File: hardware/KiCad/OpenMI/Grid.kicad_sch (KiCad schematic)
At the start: 21 parts, among them U2 MCP6002-SN

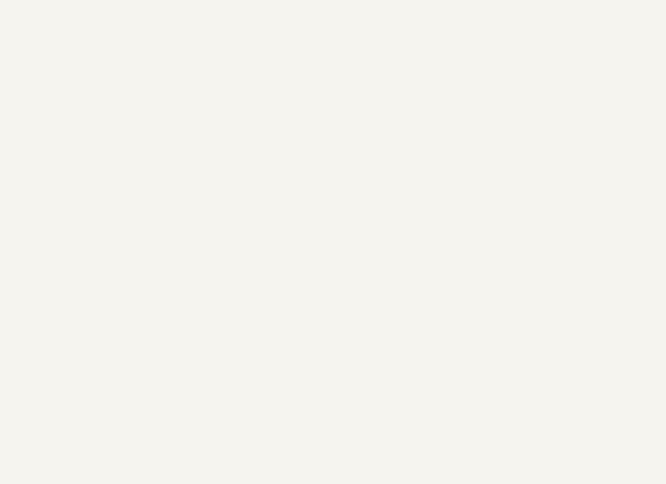
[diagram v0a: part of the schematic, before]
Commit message: feat: Adds surge and burst protection
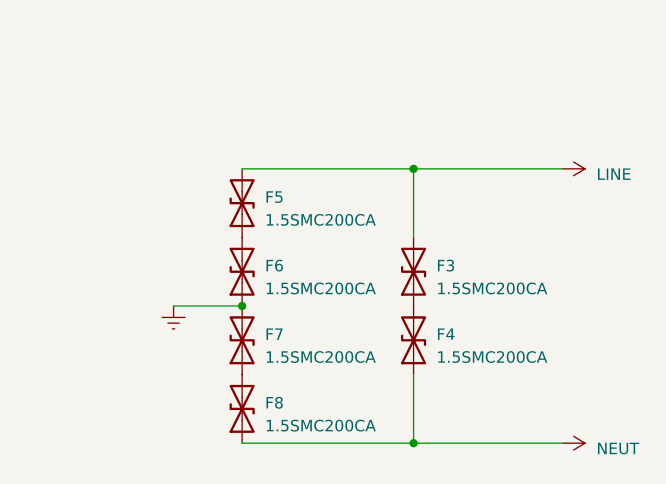
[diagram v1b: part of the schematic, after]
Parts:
- added F3, F4, F5, F6, F7, F8: 1.5SMC200CA, Diode_SMD:D_SMC, symbol _Diode_TVS:1.5SMC200CA
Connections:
- net LINE: now also F3.2 (A2), F5.2 (A2)
- net NEUT: now also F4.1 (A1), F8.1 (A1)
- new net: F7.1 (A1), F8.2 (A2)
- new net: F5.1 (A1), F6.2 (A2)
- new net: F3.1 (A1), F4.2 (A2)
- new net Earth: F6.1 (A1), F7.2 (A2)

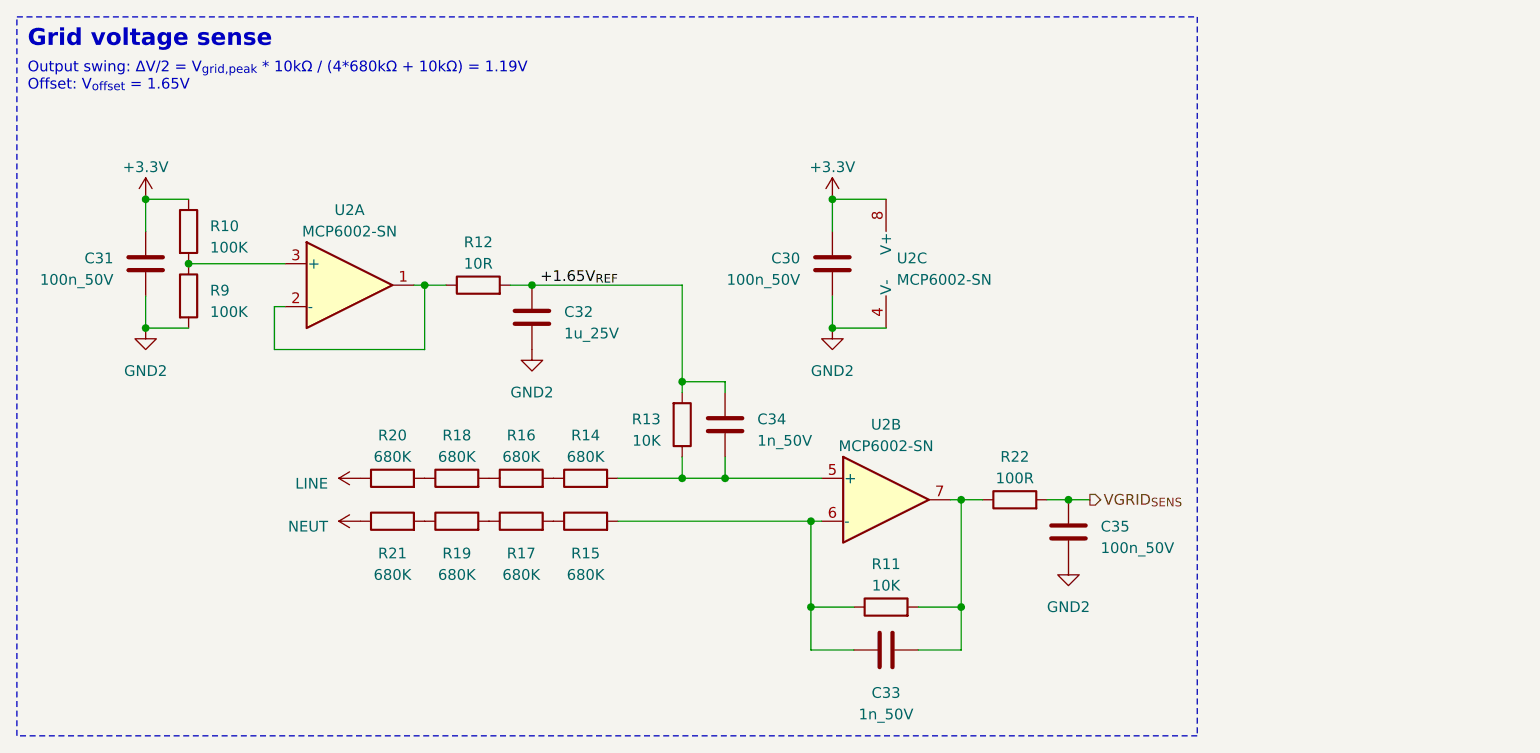
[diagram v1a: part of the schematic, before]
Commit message: feat: Add second grid voltage sens output.
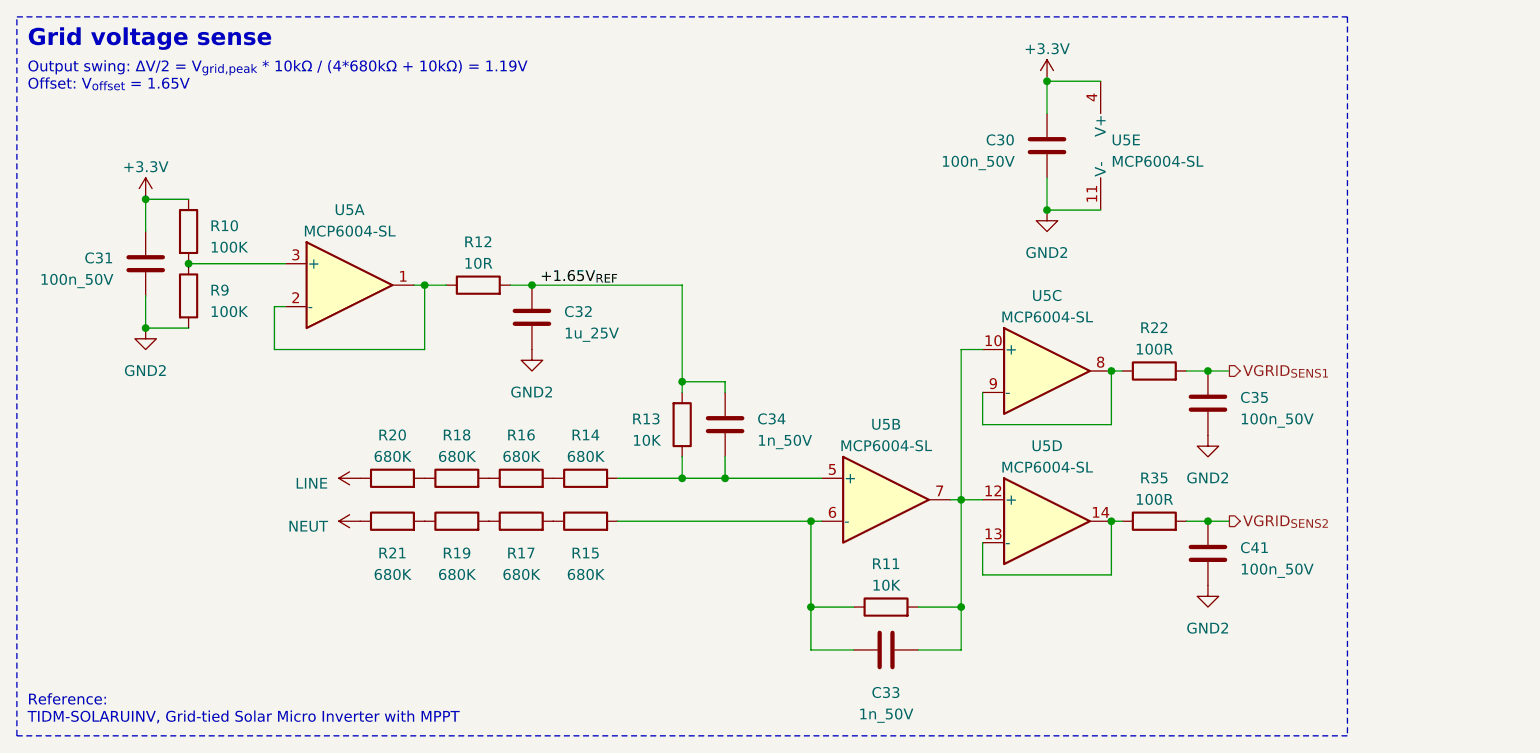
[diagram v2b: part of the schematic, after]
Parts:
- removed U2: MCP6002-SN, Package_SO:SOIC-8_3.9x4.9mm_P1.27mm, symbol _Amplifier_Operational:MCP6002-SN
- added C41: 100n_50V, Capacitor_SMD:C_0603_1608Metric, symbol _C_0603:100n_50V
- added R35: 100R, Resistor_SMD:R_0603_1608Metric, symbol _R_0603:100R
- added U5: MCP6004-SL, Package_SO:SOIC-14_3.9x8.7mm_P1.27mm, symbol _Amplifier_Operational:MCP6004-SL
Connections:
- net +3.3V: now also U5.4 (V+)
- net GND2: now also C41.2, U5.11 (V-)
- net at C34.1, R13.1, R14.2: now also U5.5 (+)
- net at R10.2, R9.1: now also U5.3 (+)
- net at C33.1, R11.1, R15.2: now also U5.6 (-)
- net at R12.1: now also U5.1, U5.2 (-)
- net at C33.2, R11.2: now also U5.10 (+), U5.12 (+), U5.7; no longer R22.1
- net VGRID_{SENS} renamed VGRID_{SENS1}
- new net: R35.1, U5.13 (-), U5.14
- new net: R22.1, U5.8, U5.9 (-)
- new net VGRID_{SENS2}: C41.1, R35.2
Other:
- note added: "Reference: TIDM-SOLARUINV, Grid-tied Solar Micro Inverter with MPPT"
- moved on the sheet: C30, C35, R22

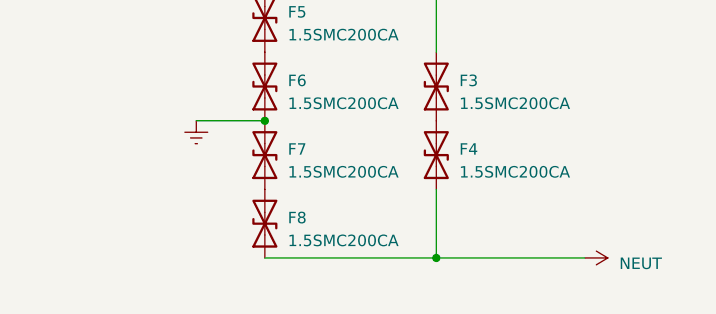
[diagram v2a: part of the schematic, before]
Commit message: docs(hw): Adds TODO to Grid sheet.
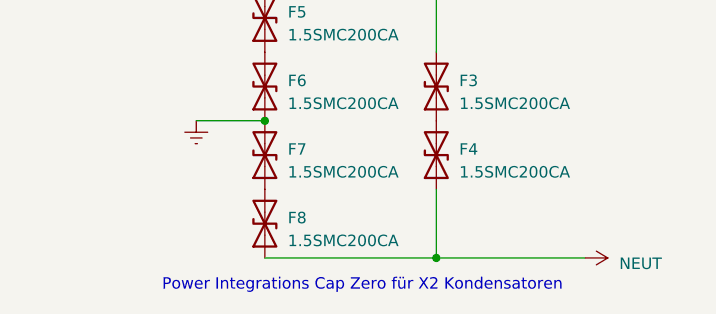
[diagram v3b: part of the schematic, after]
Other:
- note added: "Power Integrations Cap Zero für X2 Kondensatoren"
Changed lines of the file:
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@@
     (effects (font (size 1.27 1.27)) (justify left bottom))
+  )
+  (text "Power Integrations Cap Zero für X2 Kondensatoren" (at 199.39 100.33 0)
+    (effects (font (size 1.27 1.27) (color 255 0 0 1)) (justify left bottom))
   )
   (label "+1.65V_{REF}" (at 85.09 45.72 180) (fields_autoplaced)

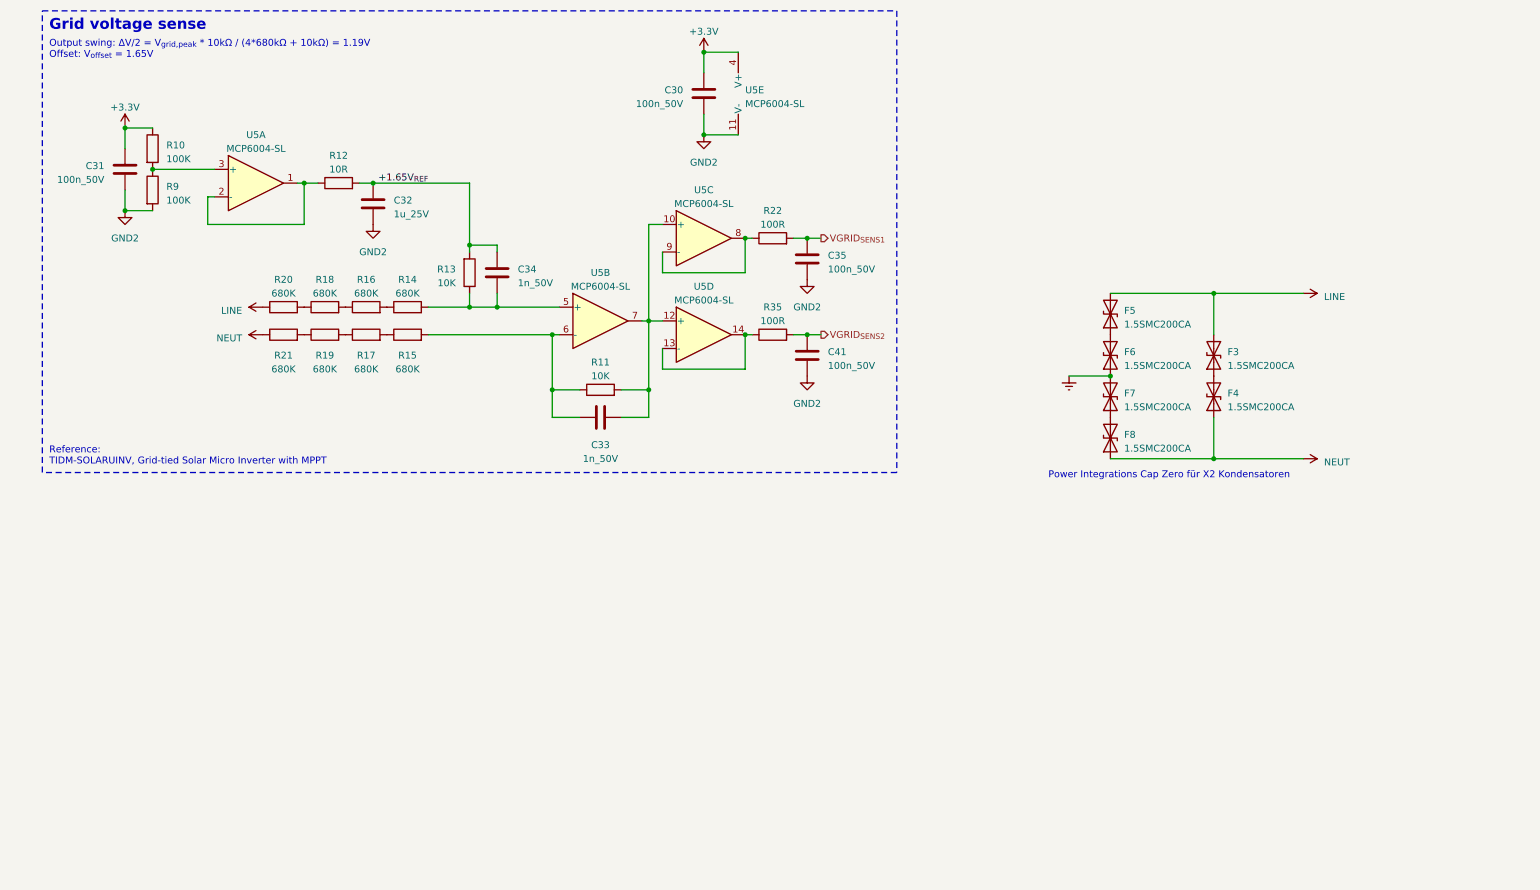
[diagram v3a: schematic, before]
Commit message: feat(hw): Adds grid-connected EMI filter, adds power relay
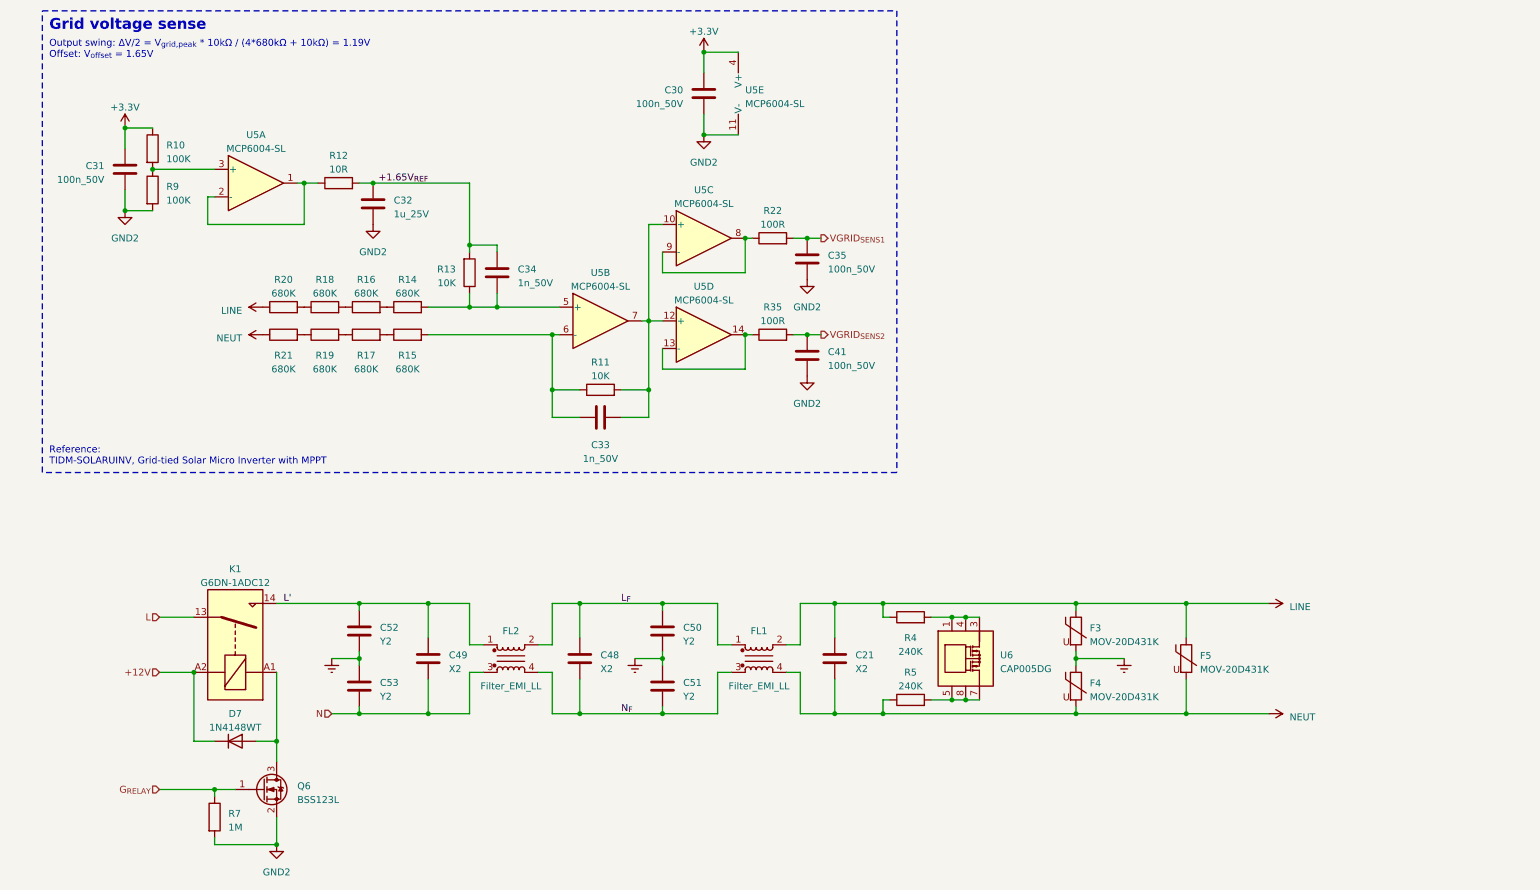
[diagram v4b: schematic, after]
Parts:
- removed F3, F4, F5, F6, F7, F8: 1.5SMC200CA, Diode_SMD:D_SMC, symbol _Diode_TVS:1.5SMC200CA
- added C21, C48, C49: X2, symbol Device:C
- added C50, C51, C52, C53: Y2, symbol Device:C
- added D7: 1N4148WT, Diode_SMD:D_0603_1608Metric, symbol _Diode:1N4148WT
- added F3, F4, F5: MOV-20D431K, Varistor:RV_Disc_D21.5mm_W5.6mm_P10mm, symbol _Varistor:MOV-20D431K
- added FL1, FL2: Filter_EMI_LL, symbol Device:Filter_EMI_LL
- added K1: G6DN-1ADC12, OpenCE:Relay_SPST_Omron_G6DN-1A, symbol _Relay:G6DN-1ADC12
- added Q6: BSS123L, Package_TO_SOT_SMD:SOT-23, symbol _Transistor_FET:BSS123L
- added R4, R5: 240K, Resistor_SMD:R_1206_3216Metric, symbol _R_1206:240K
- added R7: 1M, Resistor_SMD:R_0603_1608Metric, symbol _R_0603:1M
- added U6: CAP005DG, Package_SO:SOIC-8_3.9x4.9mm_P1.27mm, symbol _Power_Management:CAP005DG
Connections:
- net Earth: now also C50.2, C51.1, C52.2, C53.1, F3.2, F4.1
- net GND2: now also Q6.2 (S), R7.2
- net LINE: now also C21.1, F3.1, F5.1, FL1.2, R4.1
- net NEUT: now also C21.2, F4.2, F5.2, FL1.4, R5.1
- new net: D7.2 (A), K1.A1, Q6.3 (D)
- new net: R4.2, U6.1, U6.2, U6.3, U6.4
- new net: R5.2, U6.5, U6.6, U6.7, U6.8
- new net +12V: D7.1 (K), K1.A2
- new net G_{RELAY}: Q6.1 (G), R7.1
- new net L: K1.13
- new net L': C49.1, C52.1, FL2.1, K1.14
- new net L_{F}: C48.1, C50.1, FL1.1, FL2.2
- new net N: C49.2, C53.2, FL2.3
- new net N_{F}: C48.2, C51.2, FL1.3, FL2.4
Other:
- note removed: "Power Integrations Cap Zero für X2 Kondensatoren"

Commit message: refactor(hw): Adds final common mode chokes.
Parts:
- removed FL1, FL2: Filter_EMI_LL, symbol Device:Filter_EMI_LL
- added FL3: 744841330, Inductor_THT:L_CommonMode_Wuerth_WE-CMB-XS, symbol _Filter:744841330
- added FL4: 744822301, Inductor_THT:L_CommonMode_Wuerth_WE-CMB-S, symbol _Filter:744822301
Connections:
- net L': now also FL3.1
- net LINE: now also FL4.2
- net L_{F}: now also FL3.2, FL4.1
- net N: now also FL3.3
- net NEUT: now also FL4.4
- net N_{F}: now also FL3.4, FL4.3
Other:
- note added: "High frequency filter"
- note added: "Low frequency filter"
- note added: "X2: 0.1 - 0.33uF Y2: 1.0 - 2.2nF"
